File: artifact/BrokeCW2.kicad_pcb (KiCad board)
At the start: 2 copper layers, 44 parts, among them J1 Barrel_Jack_MountingPin, J10 AudioJack3_Radio, J2 Conn_Coaxial, J3 AudioJack3_Ground, J4 AudioJack3_Ground, J6 Conn_01x03_Pin, J7 Conn_01x15_PinLeft, J8 Conn_01x15_PinRight, J9 AudioJack3_Key, Q1 9013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

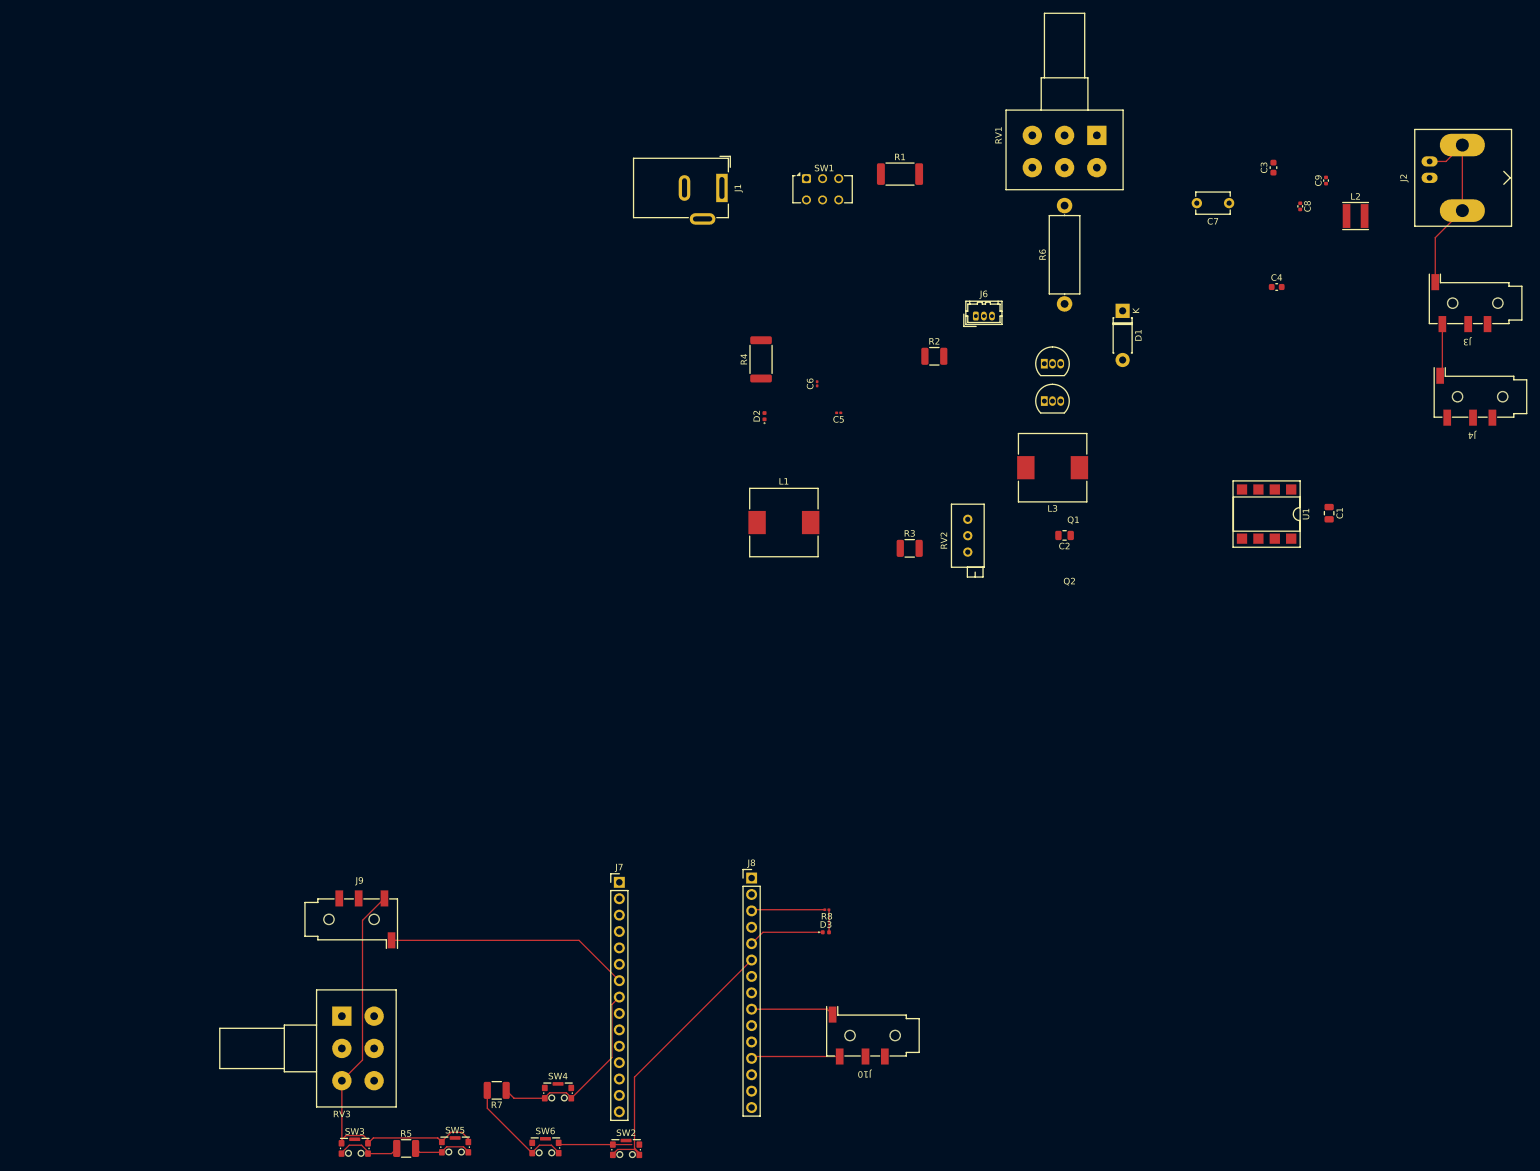
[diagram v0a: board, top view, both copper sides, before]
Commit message: reorganised the files
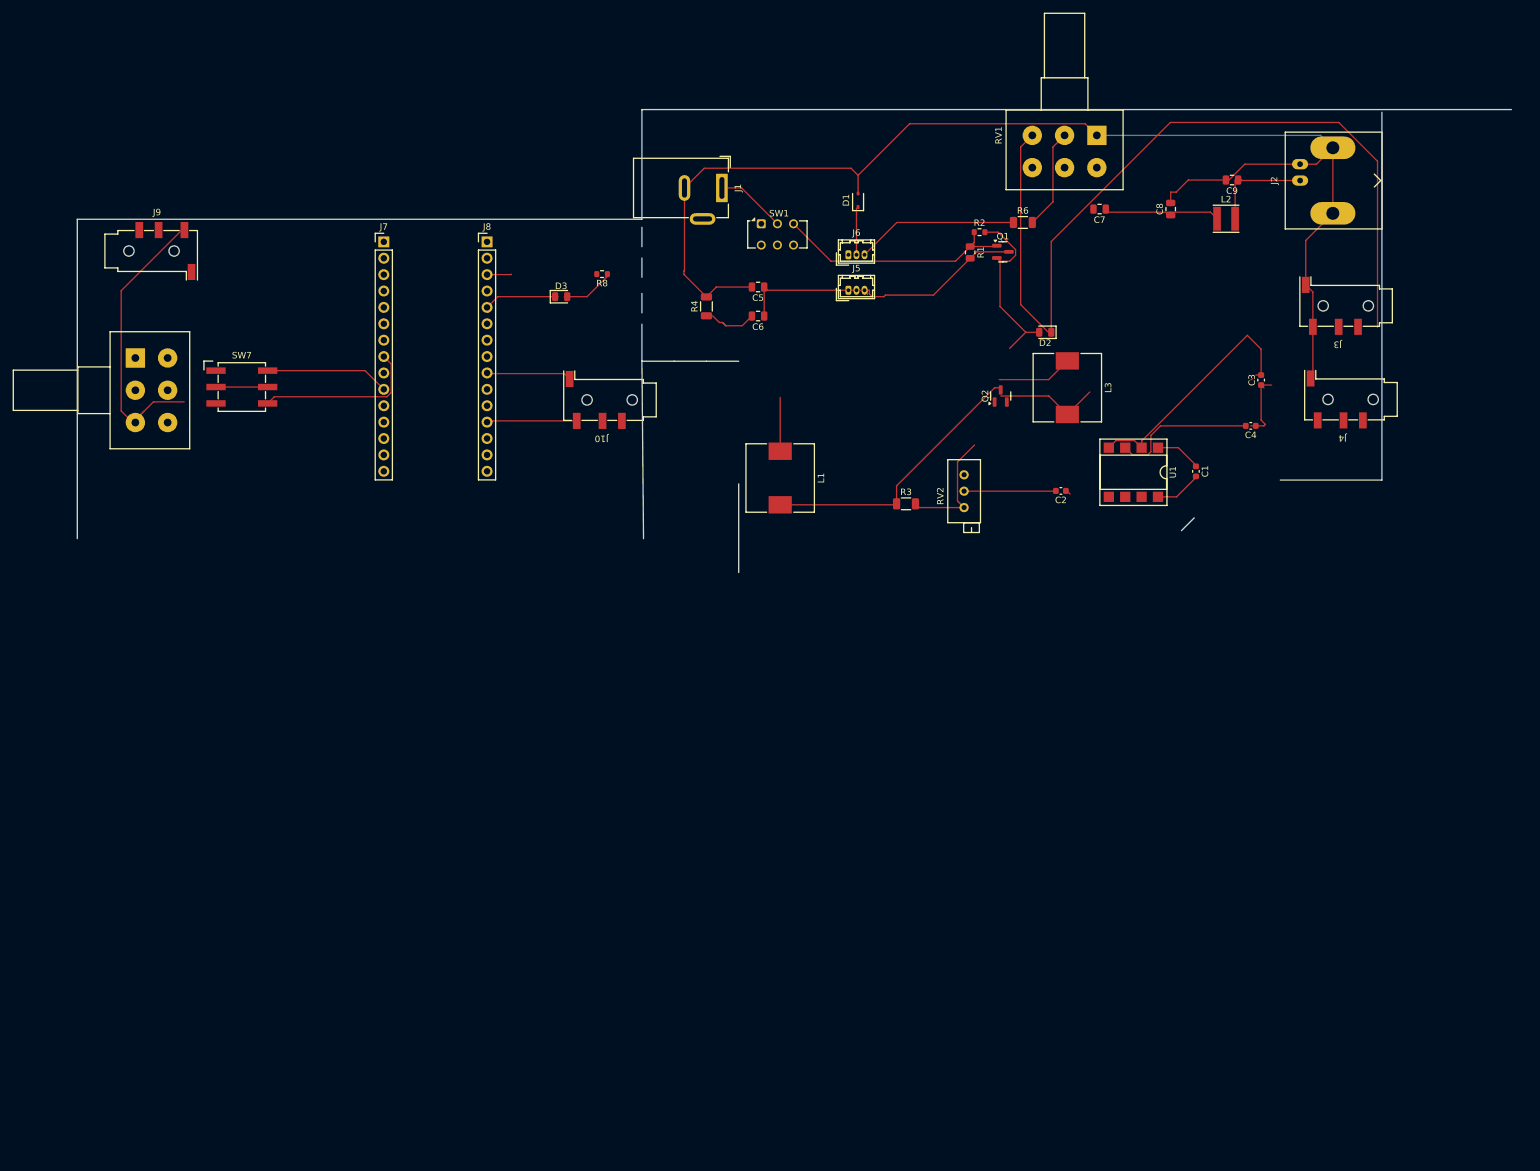
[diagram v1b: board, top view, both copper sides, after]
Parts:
- removed R5, R7: R10K, Resistor_SMD:R_1210_3225Metric
- removed SW2, SW3, SW4, SW5, SW6: CK_KMS2xxGP, Button_Switch_SMD:SW_SPST_CK_KMS2xxGP
- added J5: Conn_01x03_Pin, Connector_Hirose:Hirose_DF13-03P-1.25DSA_1x03_P1.25mm_Vertical, F.Cu at (157.5, 59.0)
- added SW7: SW_Coded_SH-7050, Button_Switch_SMD:Nidec_Copal_SH-7010B, F.Cu at (63.5, 74.0)
- C1, C2: footprint Capacitor_SMD:C_0805_2012Metric -> Capacitor_SMD:C_0603_1608Metric
- C3, C4: value C0.1uF -> C
- C5, C6: footprint Capacitor_SMD:C_0201_0603Metric -> Capacitor_SMD:C_0805_2012Metric
- C7: footprint Capacitor_THT:C_Disc_D5.1mm_W3.2mm_P5.00mm -> Capacitor_SMD:C_0805_2012Metric
- C8, C9: footprint Capacitor_SMD:C_0402_1005Metric -> Capacitor_SMD:C_0805_2012Metric
- D1: footprint Diode_THT:D_DO-41_SOD81_P7.62mm_Horizontal -> Diode_SMD:D_SOD-323
- D2, D3: footprint LED_SMD:LED_0402_1005Metric -> LED_SMD:LED_0805_2012Metric
- Q1, Q2: footprint Package_TO_SOT_THT:TO-92_Inline -> Package_TO_SOT_SMD:SOT-23
- R1: footprint Resistor_SMD:R_2512_6332Metric -> Resistor_SMD:R_0805_2012Metric
- R2: footprint Resistor_SMD:R_1210_3225Metric -> Resistor_SMD:R_0603_1608Metric
- R3: footprint Resistor_SMD:R_1210_3225Metric -> Resistor_SMD:R_1206_3216Metric
- R4: footprint Resistor_SMD:R_2512_6332Metric -> Resistor_SMD:R_1206_3216Metric
- R6: footprint Resistor_THT:R_Axial_DIN0414_L11.9mm_D4.5mm_P15.24mm_Horizontal -> Resistor_SMD:R_1206_3216Metric
- R8: value R_Small -> R; footprint Resistor_SMD:R_0201_0603Metric -> Resistor_SMD:R_0603_1608Metric
- moved J9 108.1 mm to (50.8, 52.9)
- moved RV3 106.9 mm to (47.0, 69.5)
- moved J8 106.8 mm to (101.5, 51.5)
- moved D3 106.7 mm to (113.0, 60.0)
- moved J10 106.6 mm to (119.2, 76.0)
- moved J7 105.8 mm to (85.5, 51.5)
- moved R8 104.5 mm to (119.3, 56.5)
- moved D2 45.4 mm to (188.0, 65.5), turned to 180 degrees
- moved D1 44.4 mm to (159.0, 45.0), turned to 90 degrees
- moved C3 33.0 mm to (221.5, 72.9)
- moved C5 23.2 mm to (143.5, 58.5)
- moved J6 21.9 mm to (157.5, 53.5)
- moved C4 21.9 mm to (219.9, 80.0), turned to 180 degrees
- moved U1 21.6 mm to (201.7, 87.2)
- moved C1 21.6 mm to (211.4, 87.1)
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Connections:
- C5 pad 2: Net-(D2-A) -> Net-(D1-A)
- C6 pad 2: Net-(D1-A) -> Net-(D2-A)
- J7 pad 10: unconnected-(J7-Pin_10-Pad10) -> Net-(J7-Pin_10)
- J7 pad 12: unconnected-(J7-Pin_12-Pad12) -> Net-(J7-Pin_12)
- J7 pad 4: unconnected-(J7-Pin_4-Pad4) -> Net-(J7-Pin_4)
- J7 pad 5: unconnected-(J7-Pin_5-Pad5) -> Net-(J7-Pin_5)
- J8 pad 6: Net-(J8-Pin_6) -> unconnected-(J8-Pin_6-Pad6)
- J9 pad T: Net-(J9-PadG) -> Net-(J7-Pin_12)
- RV3 pad 1: unconnected-(RV3-Pad1) -> Net-(J7-Pin_10)
- RV3 pad 2: unconnected-(RV3-Pad2) -> Net-(J7-Pin_5)
- RV3 pad 3: Net-(J9-PadG) -> Net-(J7-Pin_12)
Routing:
- net Net-(D1-A): track 37.3 -> 263.0 mm
- net Net-(D2-K): track 0.00 -> 188.1 mm
- net Net-(J9-PadG): track 75.6 -> 0.00 mm
- net Net-(D2-A): track 0.00 -> 57.2 mm
- net Net-(J7-Pin_12): track 0.00 -> 54.3 mm
- net Net-(J5-Pin_1): track 0.00 -> 47.6 mm
- net Net-(J8-Pin_6): track 43.0 -> 0.00 mm
- net Net-(J7-Pin_7): track 37.9 -> 0.00 mm
- net Net-(Q1-C): track 0.00 -> 37.4 mm
- net Net-(D1-K): track 0.00 -> 32.9 mm
- net Net-(U1-+): track 0.00 -> 22.5 mm
- net Net-(J7-Pin_10): track 0.00 -> 19.2 mm
- net Net-(R7-Pad2): track 17.8 -> 0.00 mm
- net Net-(C7-Pad1): track 0.00 -> 17.6 mm
- net Net-(Q2-C): track 0.00 -> 16.4 mm
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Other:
- board outline added: 222.2 x 71.8 mm
